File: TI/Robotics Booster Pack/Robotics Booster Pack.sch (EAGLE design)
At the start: 110 parts, among them J1 1X2.PTS, U1 TS3A44159.RGT, U10 74LVTH125.RGY, U11 SCHA4B0400, U12 BLUETOOTH-RN41", U13 XBEE-1XBEE-1_LOCK, U14 TPS54X0, U2 TPS62082.DSG, U3 DRV8800, U4 DRV8800, U5 DRV8800, U6 DRV8800, U7 PCA9557.RGV, U8 MPU-6050, U9 INA220.DGS

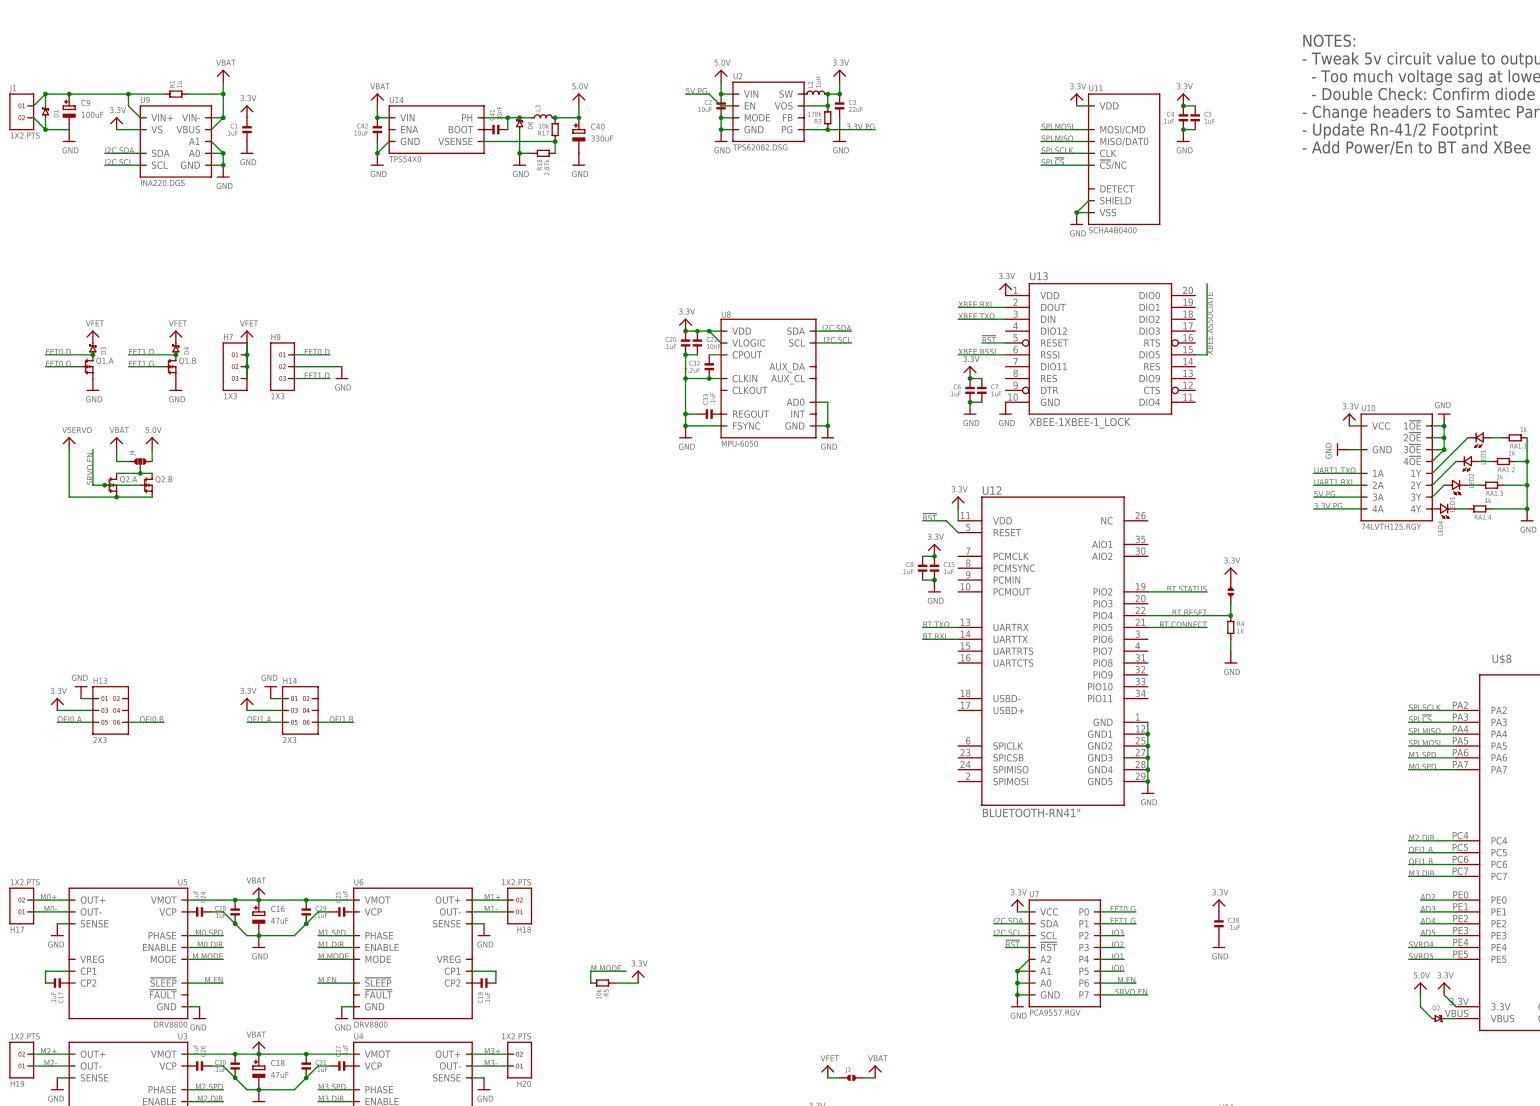
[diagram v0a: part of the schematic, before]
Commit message: Modifed Robotics BP regulators, along with a few other things
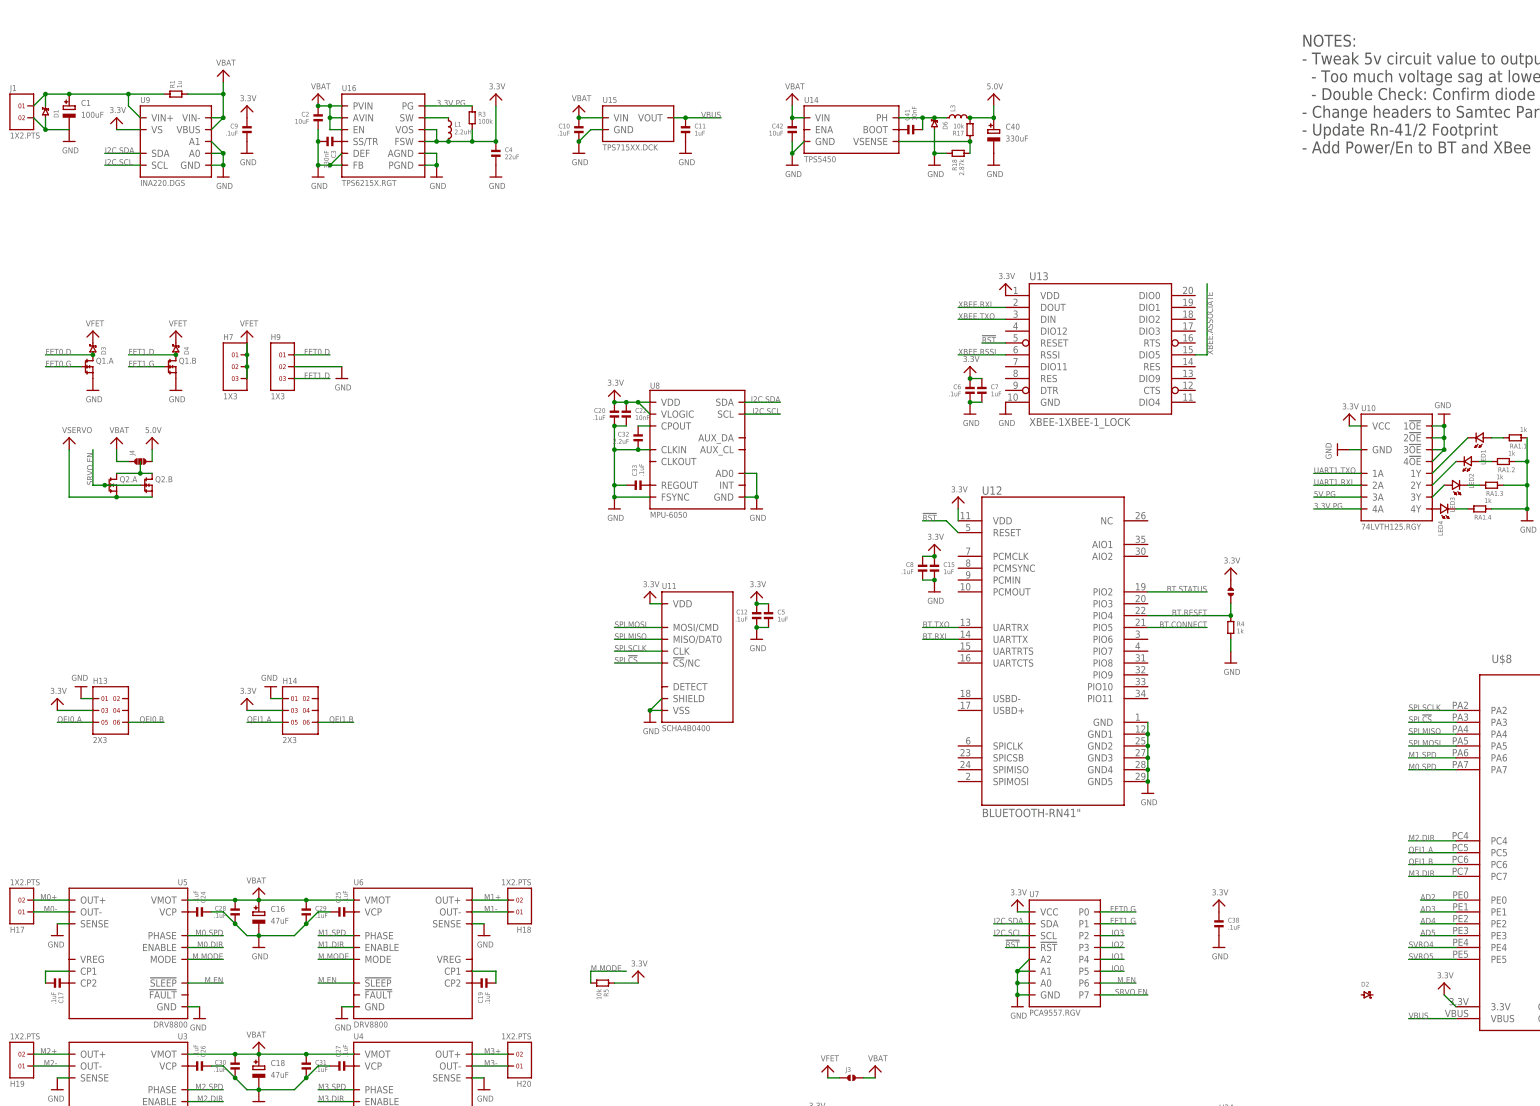
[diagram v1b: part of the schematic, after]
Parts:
- removed L2: 1uH, bourns:INDUCTOR-SRN3015
- removed U2: TPS62082.DSG, packages(ti):TPS6208X.DSG
- added C10, C12: .1uF, standardparts:CAPACITOR.0603
- added C11: 1uF, standardparts:CAPACITOR.0603
- added L1: 2.2uH, coilcraft:INDUCTOR.XAL4020
- added U15: TPS715XX.DCK, packages(ti):TPS715XX.DCK
- added U16: TPS6215X.RGT, packages(ti):TPS6215X.RGT
- C1: value .1uF -> 100uF; device standardparts:CAPACITOR.0603 -> microbuilder:CAP_ELECTROLYTICPANASONIC_D
- C2: device standardparts:CAPACITOR.0603 -> standardparts:CAPACITOR.1206
- C3: value 22uF -> 330nF
- C4: value .1uF -> 22uF; device standardparts:CAPACITOR.0603 -> standardparts:CAPACITOR.0805
- C9: value 100uF -> .1uF; device microbuilder:CAP_ELECTROLYTICPANASONIC_D -> standardparts:CAPACITOR.0603
- L3: value INDUCTOR.XAL6060 -> (none)
- R3: value 178k -> 100k
- U14: value TPS54X0 -> TPS5450
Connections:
- removed net N$12: L2.1, U2.SW
- new net N$23: C3.1, U16.SS/TR
- new net VBUS: C11.1, U$8.VBUS, U15.VOUT
- net 3.3V: now also C12.1, C9.1, L1.2, U16.FSW, U16.VOS; no longer C1.1, C3.1, L2.2, U2.VOS
- net 3.3V.PG: now also U16.PG; no longer U2.PG
- net 5.0V: no longer C2.1, D2.2, U2.VIN
- net 5V.PG: no longer U2.EN
- net GND: now also C10.2, C11.2, C12.2, C9.2, U15.GND, U16.AGND, U16.DEF, U16.FB, U16.PGND; no longer C1.2, U2.GND, U2.MODE
- net N$1: now also L1.1, U16.SW; no longer D2.1, U$8.VBUS
- net N$22: now also C1.+; no longer C9.+
- net VBAT: now also C10.1, C2.1, U15.VIN, U16.AVIN, U16.EN, U16.PVIN
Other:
- moved on the sheet: C2, C20, C22, C3, C32, C33, C4, C40, C41, C42, C5, D2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

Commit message: Cleaned up Servo.EN connections and indicator LEDs Routing will soon begin. It's unreasonable to believe that it will all be complete by the end of the weekend, bu some goals aren't meant to be met.
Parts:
- removed D2: CDBMT2100-HF, comchip:CDBMT____-HF
- removed R3: 100k, standardparts:RESISTOR.0603
- added R8: 10k, standardparts:RESISTOR.0603
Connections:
- removed net 3.3V.PG: R3.1, U10.4A, U16.PG
- removed net 5V.PG: U10.3A
- removed net N$28: LED1.2, U10.1Y
- new net N$12: LED4.2, RA1.2.2
- new net SVRO.EN: Q2.A.G, Q2.B.G, R8.1
- net 3.3V: now also U10.1A; no longer R3.2
- net 5.0V: now also U10.2A
- net GND: now also R8.2
- net IO0: now also U7.P7; no longer U7.P5
- net IO1: now also U7.P6; no longer U7.P4
- net IO2: now also U7.P5; no longer U7.P3
- net IO3: now also U7.P4; no longer U7.P2
- net M.EN: now also U10.4A, U7.P3; no longer U7.P6
- net N$10: now also U10.2Y; no longer RA1.2.2
- net N$11: now also U10.1Y; no longer RA1.1.2
- net N$26: now also LED3.2, RA1.1.2; no longer LED2.2, U10.2Y
- net N$5: now also LED1.2; no longer LED4.2
- net N$8: now also LED2.2; no longer LED3.2
- net SRVO.EN: now also U10.3A, U7.P2; no longer Q2.A.G, Q2.B.G, U7.P7
- net UART0.RXI: now also U$15.2
- net UART0.TXO: now also U$15.1
- net UART1.RXI: no longer U10.2A
- net UART1.TXO: no longer U10.1A
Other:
- moved on the sheet: C10, C11, C2, C3, C4, C40, C41, C42, D6, L1, L3, LED1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

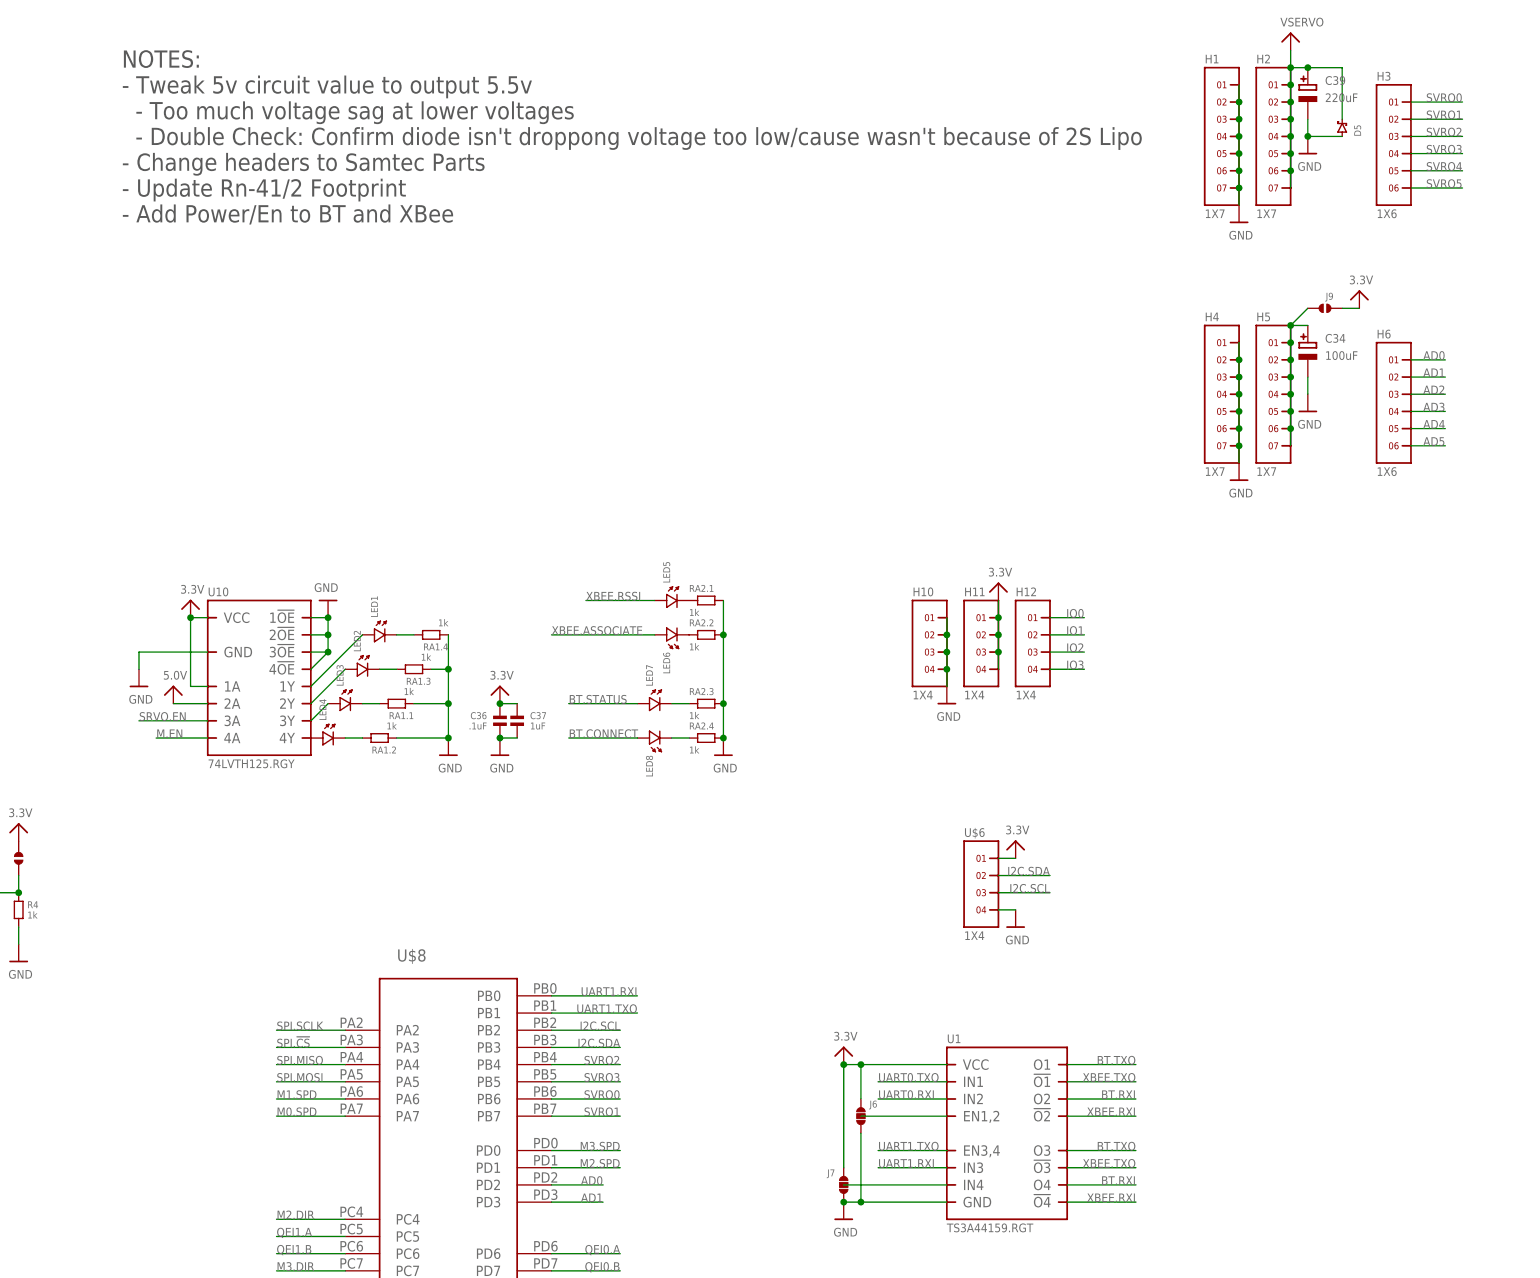
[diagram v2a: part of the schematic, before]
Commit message: Began routing of Robotics BP v2 Bluetooth, XBee, and UART mux routing nearly complete. Started LEDs and IMU routing.
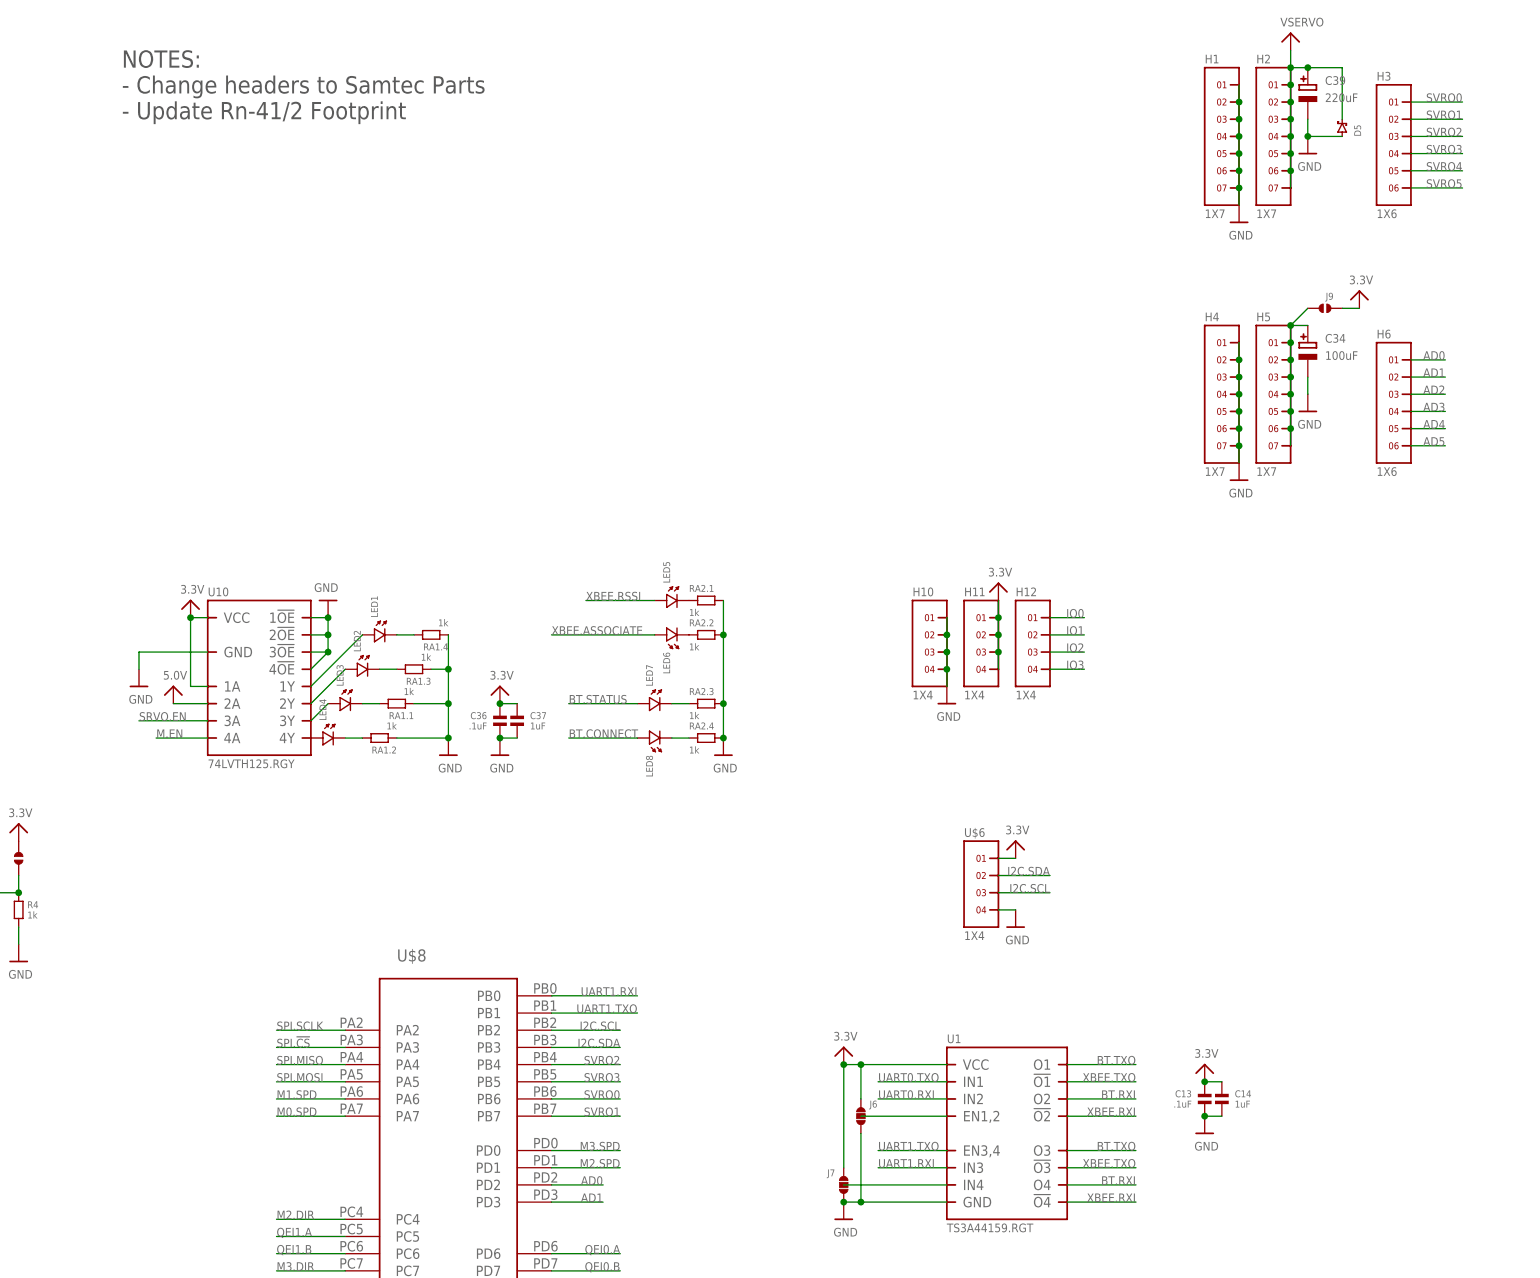
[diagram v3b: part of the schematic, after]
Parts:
- added C13: .1uF, standardparts:CAPACITOR.0603
- added C14: 1uF, standardparts:CAPACITOR.0603
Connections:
- net 3.3V: now also C13.1, C14.1
- net GND: now also C13.2, C14.2
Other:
- note added: "NOTES: - Change headers to Samtec Parts - Update Rn-41/2 Footprint"
- note removed: "NOTES: - Tweak 5v circuit value to output 5.5v - Too much voltage sag at lower voltages - Double Check: Confirm diode isn't droppong voltage too low/cause wasn't because of 2S Lipo - Change headers to Samtec Parts - Update Rn-41/2 Footprint - Add Power/En to BT and XBee"
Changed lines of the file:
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@@
 <part name="U$68" library="microbuilder" deviceset="GND" device=""/>
 <part name="U$73" library="microbuilder" deviceset="5.0V" device=""/>
+<part name="U$20" library="microbuilder" deviceset="3.3V" device=""/>
+<part name="U$75" library="microbuilder" deviceset="GND" device=""/>
+<part name="C13" library="standardparts" deviceset="CAPACITOR" device=".0603" value=".1uF"/>
+<part name="C14" library="standardparts" deviceset="CAPACITOR" device=".0603" value="1uF"/>
 </parts>
 <sheets>
@@
 <plain>
 <text x="284.48" y="251.46" size="2.54" layer="97" align="top-left">NOTES:
-- Tweak 5v circuit value to output 5.5v
-  - Too much voltage sag at lower voltages
-  - Double Check: Confirm diode isn't droppong voltage too low/cause wasn't because of 2S Lipo
 - Change headers to Samtec Parts
-- Update Rn-41/2 Footprint
-- Add Power/En to BT and XBee</text>
+- Update Rn-41/2 Footprint</text>
 </plain>
 <instances>
@@
 <instance part="U$68" gate="G$1" x="33.02" y="147.32"/>
 <instance part="U$73" gate="G$1" x="292.1" y="157.48"/>
+<instance part="U$20" gate="G$1" x="444.5" y="101.6"/>
+<instance part="U$75" gate="G$1" x="444.5" y="91.44"/>
+<instance part="C13" gate="G$1" x="444.5" y="96.52" rot="MR270"/>
+<instance part="C14" gate="G$1" x="447.04" y="96.52" rot="R270"/>
 </instances>
 <busses>
@@
 <junction x="332.74" y="149.86"/>
 </segment>
+<segment>
+<pinref part="C13" gate="G$1" pin="2"/>
+<pinref part="U$75" gate="G$1" pin="GND"/>
+<pinref part="C14" gate="G$1" pin="2"/>
+<wire x1="444.5" y1="93.98" x2="447.04" y2="93.98" width="0.1524" layer="91"/>
+<junction x="444.5" y="93.98"/>
+</segment>
 </net>
 <net name="3.3V" class="0">
@@
 <junction x="111.76" y="233.68"/>
 </segment>
+<segment>
+<pinref part="C13" gate="G$1" pin="1"/>
+<pinref part="U$20" gate="G$1" pin="3.3V"/>
+<pinref part="C14" gate="G$1" pin="1"/>
+<wire x1="447.04" y1="99.06" x2="444.5" y2="99.06" width="0.1524" layer="91"/>
+<junction x="444.5" y="99.06"/>
+</segment>
 </net>
